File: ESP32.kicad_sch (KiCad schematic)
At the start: 25 parts, among them J1 Debug_U0, J16 USB_NATIVO, J3 RS485, J4 Uart1, U2 SP3485EN, U8 ESP32-S3-WROOM-1

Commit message: RS485 upgrades
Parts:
- added D1: SM712_SOT23, Package_TO_SOT_SMD:SOT-23, symbol Diode:SM712_SOT23
- added R4: 120, Resistor_SMD:R_0603_1608Metric, symbol Device:R
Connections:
- net GND: now also D1.3 (common)
- net RS485_A: now also D1.1 (A1), R4.1
- net RS485_B: now also D1.2 (A2), R4.2

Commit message: fixes
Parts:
- D1: value SM712_SOT23 -> SM712-02HTG; LCSC PN (none) -> C5449363; MPN (none) -> SM712-02HTG; Manufacturer (none) -> DOWO; Manufacturer Part (none) -> SM712-02HTG
- J1, J4: now left out of the parts list
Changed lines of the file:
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@@
 			)
 		)
-		(property "Value" "SM712_SOT23"
+		(property "Value" "SM712-02HTG"
 			(at 143.51 60.96 0)
 			(show_name no)
@@
 			)
 		)
-		(property "Description" "7V/12V, 600W Asymmetrical TVS Diode Array, SOT-23"
+		(property "Description" "2-channel bidirectional RS-485 TVS diode array, SOT-23"
+			(at 143.51 64.77 0)
+			(hide yes)
+			(show_name no)
+			(do_not_autoplace no)
+			(effects
+				(font
+					(size 1.27 1.27)
+				)
+			)
+		)
+		(property "Manufacturer" "DOWO"
+			(at 143.51 64.77 0)
+			(hide yes)
+			(show_name no)
+			(do_not_autoplace no)
+			(effects
+				(font
+					(size 1.27 1.27)
+				)
+			)
+		)
+		(property "Manufacturer Part" "SM712-02HTG"
+			(at 143.51 64.77 0)
+			(hide yes)
+			(show_name no)
+			(do_not_autoplace no)
+			(effects
+				(font
+					(size 1.27 1.27)
+				)
+			)
+		)
+		(property "MPN" "SM712-02HTG"
+			(at 143.51 64.77 0)
+			(hide yes)
+			(show_name no)
+			(do_not_autoplace no)
+			(effects
+				(font
+					(size 1.27 1.27)
+				)
+			)
+		)
+		(property "LCSC PN" "C5449363"
 			(at 143.51 64.77 0)
 			(hide yes)
@@
 		(in_bom no)
 		(on_board yes)
-		(in_pos_files yes)
+		(in_pos_files no)
 		(dnp no)
 		(fields_autoplaced yes)
@@
 		(body_style 1)
 		(exclude_from_sim no)
-		(in_bom yes)
+		(in_bom no)
 		(on_board yes)
-		(in_pos_files yes)
+		(in_pos_files no)
 		(dnp no)
 		(property "Reference" "J1"
@@
 		(body_style 1)
 		(exclude_from_sim no)
-		(in_bom yes)
+		(in_bom no)
 		(on_board yes)
-		(in_pos_files yes)
+		(in_pos_files no)
 		(dnp no)
 		(fields_autoplaced yes)

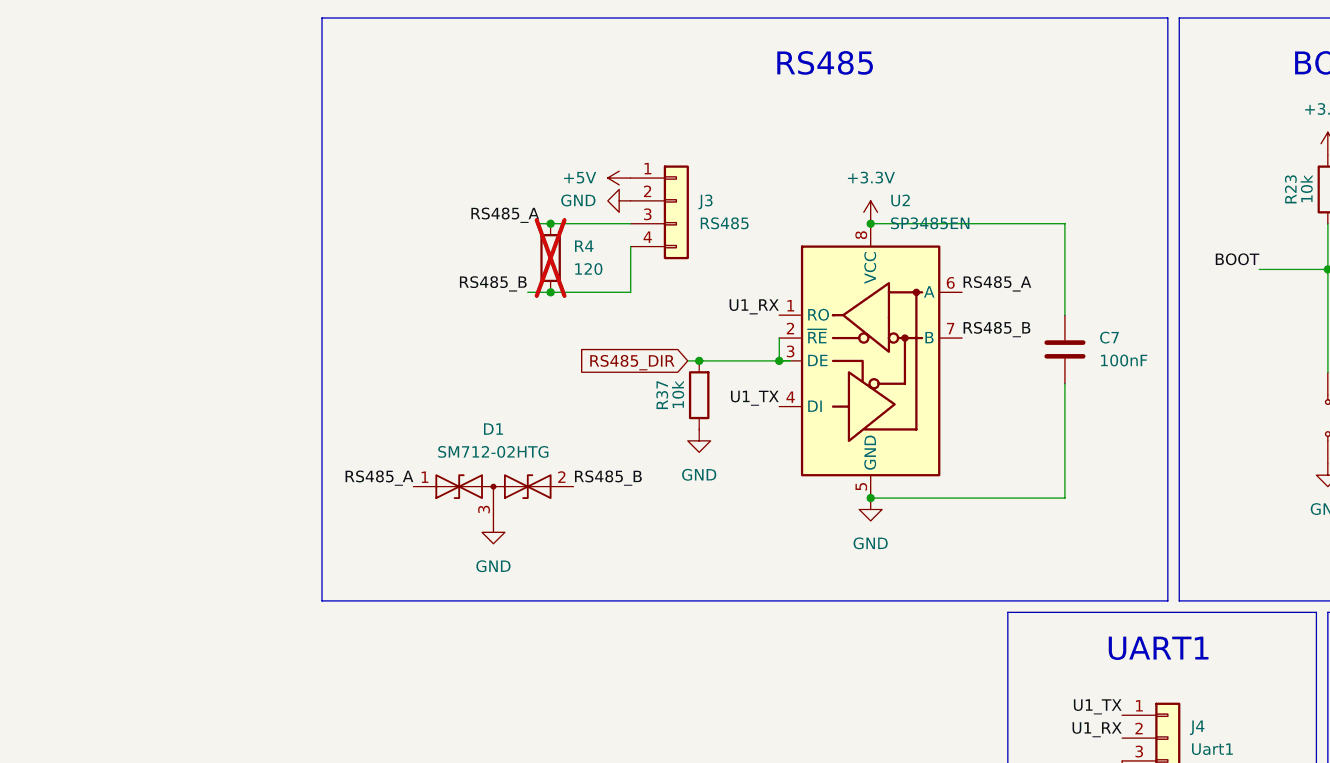
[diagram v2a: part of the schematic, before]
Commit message: add second header for rs485
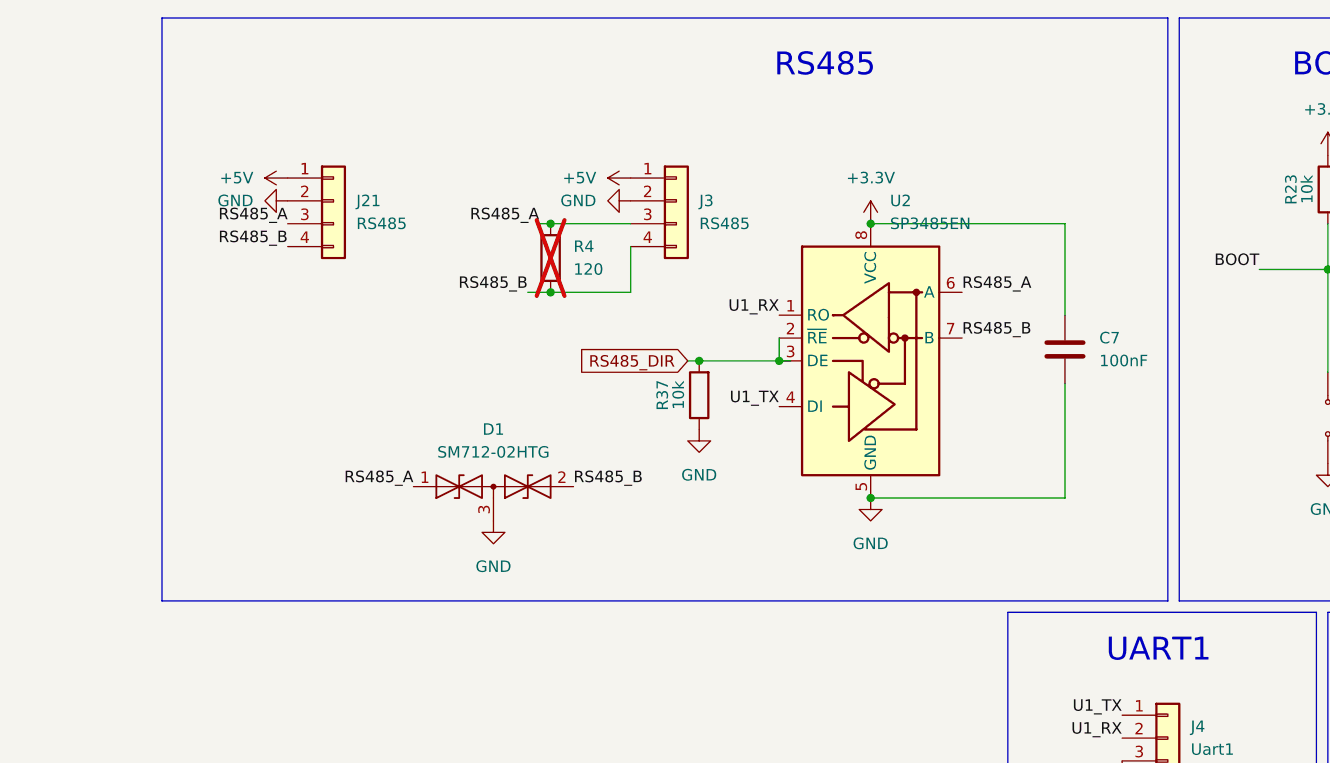
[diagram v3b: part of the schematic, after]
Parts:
- added J21: RS485, Connector_PinHeader_2.54mm:PinHeader_1x04_P2.54mm_Vertical, symbol Connector_Generic:Conn_01x04
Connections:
- net +5V: now also J21.1 (Pin_1)
- net GND: now also J21.2 (Pin_2)
- net RS485_A: now also J21.3 (Pin_3)
- net RS485_B: now also J21.4 (Pin_4)

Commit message: vias de gnd y pin header de GPIOS sobrantes
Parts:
- added J22: Conn_01x07, Connector_PinHeader_2.54mm:PinHeader_1x07_P2.54mm_Vertical, symbol Connector_Generic:Conn_01x07
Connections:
- net +3.3V: now also J22.1 (Pin_1)
- net GND: now also J22.2 (Pin_2)
- net IO3: now reaches U8.15 (IO3)
- net IO3: now also J22.5 (Pin_5)
- net IO46: now reaches U8.16 (IO46)
- net IO46: now also J22.6 (Pin_6)
- net IO47: now reaches U8.24 (IO47)
- net IO47: now also J22.3 (Pin_3)
- net IO48: now reaches U8.25 (IO48)
- net IO48: now also J22.4 (Pin_4)
- net IO45: now reaches U8.26 (IO45)
- net IO45: now also J22.7 (Pin_7)
- no-connect marks 7 -> 2

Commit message: coreccion de value j22
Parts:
- J22: value Conn_01x07 -> GPIOS_AUX
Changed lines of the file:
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@@
 			)
 		)
-		(property "Value" "Conn_01x07"
+		(property "Value" "GPIOS_AUX"
 			(at 177.8 93.9799 0)
 			(show_name no)

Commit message: Consolida pasivos Basic y valida filtro de acelerador
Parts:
- C6, C7: LCSC PN C1590 -> C14663; MPN CL10B104KA8NNNC -> CC0603KRX7R9BB104; Manufacturer Samsung Electro-Mechanics -> Yageo; Manufacturer Part CL10B104KA8NNNC -> CC0603KRX7R9BB104
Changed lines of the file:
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@@
 			)
 		)
-		(property "LCSC PN" "C1590"
+		(property "LCSC PN" "C14663"
 			(at -182.88 26.67 0)
 			(hide yes)
@@
 			)
 		)
-		(property "Manufacturer" "Samsung Electro-Mechanics"
+		(property "Manufacturer" "Yageo"
 			(at -182.88 26.67 0)
 			(hide yes)
@@
 			)
 		)
-		(property "Manufacturer Part" "CL10B104KA8NNNC"
+		(property "Manufacturer Part" "CC0603KRX7R9BB104"
 			(at -182.88 26.67 0)
 			(hide yes)
@@
 			)
 		)
-		(property "MPN" "CL10B104KA8NNNC"
+		(property "MPN" "CC0603KRX7R9BB104"
 			(at -182.88 26.67 0)
 			(hide yes)
@@
 			)
 		)
-		(property "LCSC PN" "C1590"
+		(property "LCSC PN" "C14663"
 			(at -66.04 -102.87 0)
 			(hide yes)
@@
 			)
 		)
-		(property "Manufacturer" "Samsung Electro-Mechanics"
+		(property "Manufacturer" "Yageo"
 			(at -66.04 -102.87 0)
 			(hide yes)
@@
 			)
 		)
-		(property "Manufacturer Part" "CL10B104KA8NNNC"
+		(property "Manufacturer Part" "CC0603KRX7R9BB104"
 			(at -66.04 -102.87 0)
 			(hide yes)
@@
 			)
 		)
-		(property "MPN" "CL10B104KA8NNNC"
+		(property "MPN" "CC0603KRX7R9BB104"
 			(at -66.04 -102.87 0)
 			(hide yes)

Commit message: Registra PCB SALUS v3 con montaje M3 y terminacion RS485
Conserva los dos paquetes de fabricacion del 20 de agosto, sus fuentes, checksums y validaciones. El paquete final monta R4 de 120 ohm e incluye 64 componentes SMD. Actualiza el README para identificar la entrega vigente y los limites de la validacion archivada.
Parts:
- R4: LCSC PN (none) -> C22787; MPN (none) -> 0603WAF1200T5E; Manufacturer (none) -> UNI-ROYAL; Manufacturer Part (none) -> 0603WAF1200T5E; now fitted; now in the parts list
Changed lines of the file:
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@@
 		(body_style 1)
 		(exclude_from_sim no)
-		(in_bom no)
+		(in_bom yes)
 		(on_board yes)
 		(in_pos_files yes)
-		(dnp yes)
+		(dnp no)
 		(fields_autoplaced yes)
 		(property "Reference" "R4"
@@
 			)
 		)
+		(property "MPN" "0603WAF1200T5E"
+			(at 149.86 39.37 0)
+			(hide yes)
+			(show_name no)
+			(do_not_autoplace no)
+			(effects (font (size 1.27 1.27)))
+		)
+		(property "Manufacturer" "UNI-ROYAL"
+			(at 149.86 39.37 0)
+			(hide yes)
+			(show_name no)
+			(do_not_autoplace no)
+			(effects (font (size 1.27 1.27)))
+		)
+		(property "Manufacturer Part" "0603WAF1200T5E"
+			(at 149.86 39.37 0)
+			(hide yes)
+			(show_name no)
+			(do_not_autoplace no)
+			(effects (font (size 1.27 1.27)))
+		)
+		(property "LCSC PN" "C22787"
+			(at 149.86 39.37 0)
+			(hide yes)
+			(show_name no)
+			(do_not_autoplace no)
+			(effects (font (size 1.27 1.27)))
+		)
 		(pin "2"
